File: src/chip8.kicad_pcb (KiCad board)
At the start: 2 copper layers, 43 parts, among them J1 204926-1103, M1 STM32L476RGT6, Q1 DMP2240UW-7, Q2 BC847-T, T1 5002, T2 5002, T3 5002, T4 5002, U1 MCP73831T-2ACI_OT, U2 PCM12SMTR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

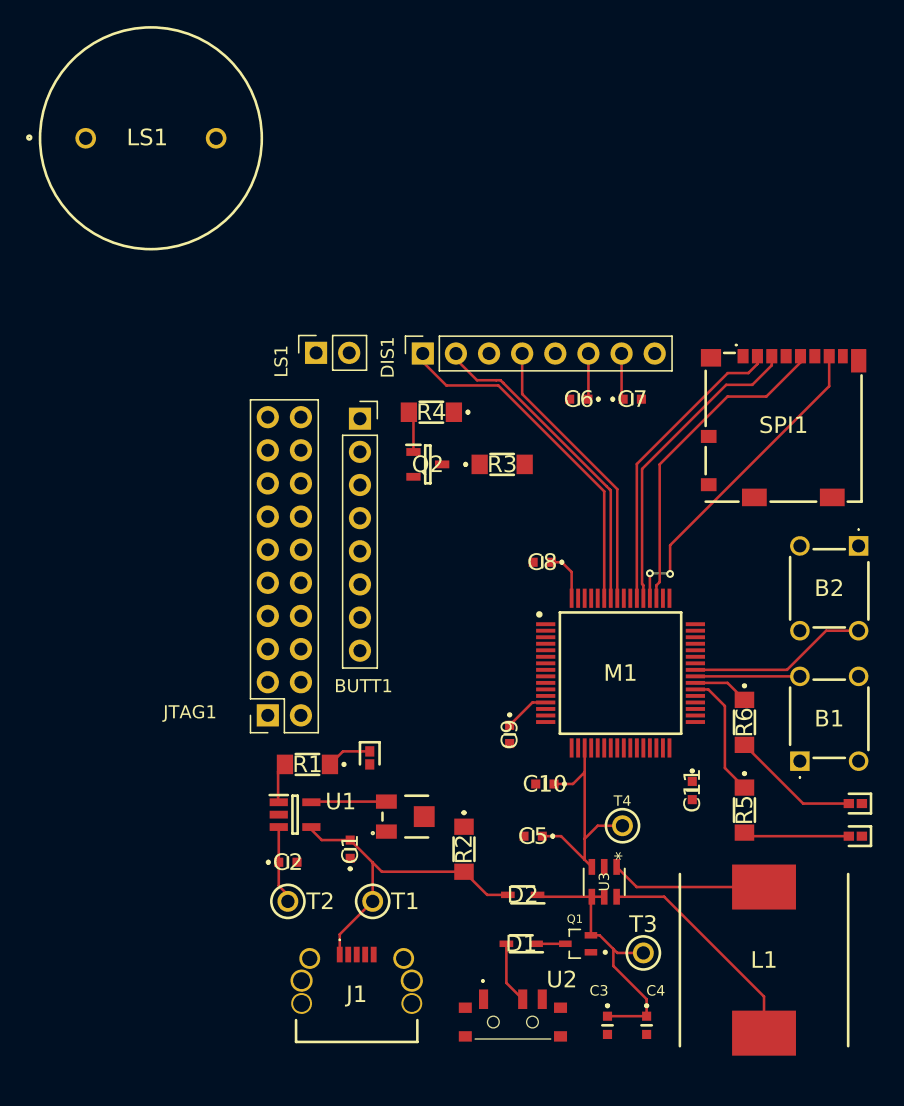
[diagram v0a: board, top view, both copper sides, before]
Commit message: ground plane and corrections done
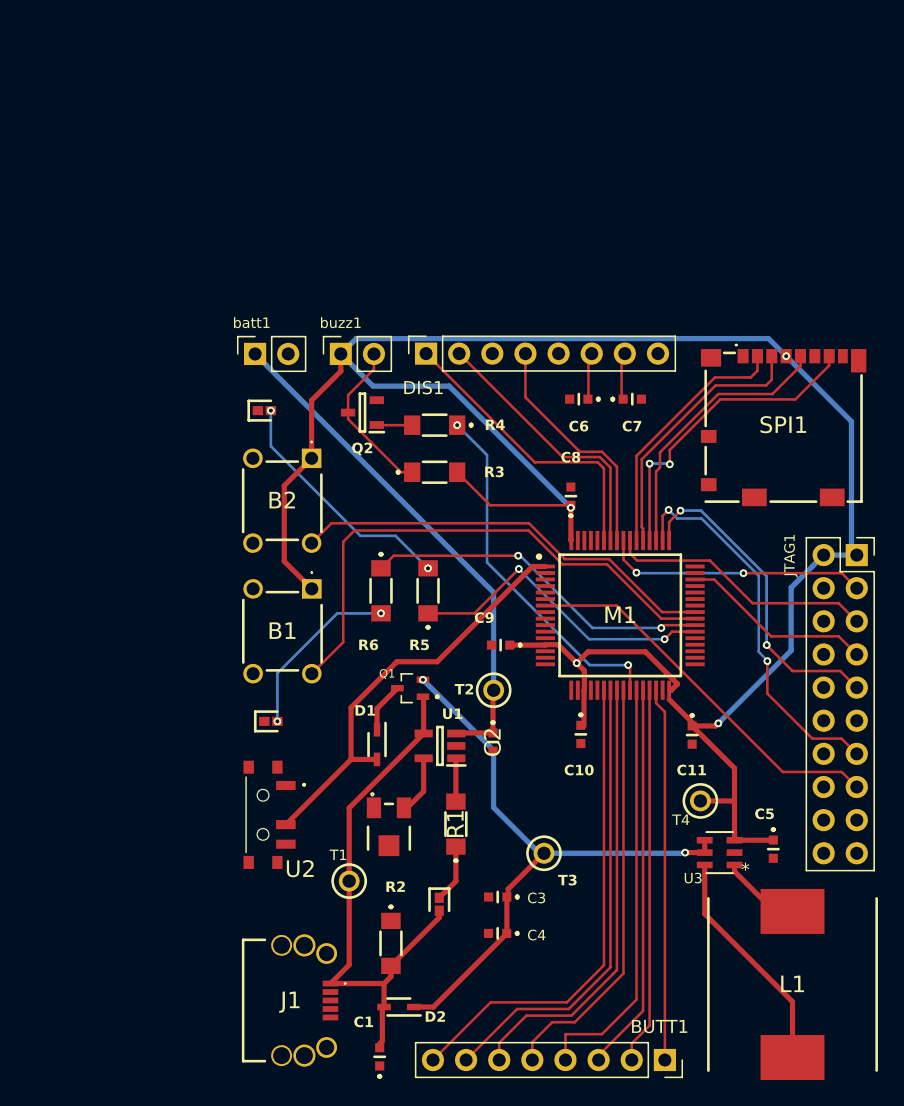
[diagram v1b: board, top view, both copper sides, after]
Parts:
- removed LS1: PS1720P02, footprints:PS17_1
- added batt1: Conn_01x02_Pin, Connector_PinSocket_2.54mm:PinSocket_1x02_P2.54mm_Vertical, F.Cu at (88.0, 73.5)
- moved LD2 55.8 mm to (88.7, 77.9), turned to 0 degrees
- moved BUTT1 54.4 mm to (119.4, 127.7), turned to -90 degrees
- moved JTAG1 46.8 mm to (134.1, 89.0), turned to 0 degrees
- moved LD3 45.2 mm to (89.2, 101.7), turned to 0 degrees
- moved B2 42.5 mm to (92.3, 81.5)
- moved B1 39.7 mm to (92.3, 91.5), turned to -90 degrees
- moved R6 29.6 mm to (97.6, 91.7)
- moved R5 29.5 mm to (101.2, 91.7), turned to 90 degrees
- moved U2 24.9 mm to (88.6, 108.9), turned to -90 degrees
- moved Q1 23.4 mm to (99.9, 99.2)
- moved T2 22.6 mm to (106.3, 99.3), turned to -90 degrees
- moved D1 18.9 mm to (97.3, 103.5), turned to -90 degrees
- moved C5 18.4 mm to (127.7, 111.5), turned to -90 degrees
- moved C2 18.2 mm to (106.2, 103.3), turned to -90 degrees
- moved C1 16.1 mm to (97.5, 127.4)
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- renumbered LS1 to buzz1
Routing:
- net /VDD: track 26.7 -> 168.3 mm, vias 0 -> 4
- net /I2C0: track 0.00 -> 37.2 mm
- net /I2C1: track 0.00 -> 35.3 mm
- net /I2C2: track 0.00 -> 34.1 mm
- net /VBAT1: track 5.86 -> 39.5 mm
- net /IO2: track 8.01 -> 41.2 mm
- net /I2C3: track 0.00 -> 31.9 mm
- net /I2C4: track 0.00 -> 31.9 mm
- net /JTAG5: track 0.00 -> 29.6 mm
- net /JTAG4: track 0.00 -> 29.6 mm, vias 0 -> 2
- net /I2C5: track 0.00 -> 29.4 mm
- net /I2C7: track 0.00 -> 28.6 mm
- net /I2C6: track 0.00 -> 28.6 mm
- net /VBAT2: track 4.77 -> 32.4 mm
- net /PB0: track 0.00 -> 27.5 mm, vias 0 -> 2
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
